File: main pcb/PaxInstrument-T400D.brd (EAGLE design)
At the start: 99.1 x 52.1 mm, 89 parts, among them IC2 NC7S00DBV, J1 MICRO-SDCARD-CONNECTOR-330006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, Q1 DMP2035U-7, U2 APX809, U3 MCP73831, U4 MIC5219-3.3V, X1 FH12-12S-1S, X2 FH12-12S-0.5SH, Y1 RESONATORSMD

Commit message: - Not sure what changed. This is still just playing around.
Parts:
- removed ICSP, ICSP1: ICSP, PaxInstrument-T400:SPARKFUN-CONNECTORS_2X3_SMT_POSTS_PAXINSTRUMENT
- added JP13, JP14, JP15, JP16, JP17: M01PTH, SparkFun-Connectors:1X01
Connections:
- net 3.3V: no longer ICSP1.6
- net DATA1: no longer ICSP1.3
- net DATA2: no longer ICSP1.4
- net GND: no longer ICSP.6, ICSP1.5
- net MISO: now also JP13.1; no longer ICSP.1
- net MOSI: now also JP17.1; no longer ICSP.4
- net RESET: now also JP15.1; no longer ICSP.5
- net SCK: now also JP14.1; no longer ICSP.3
- net SCL: no longer ICSP1.1
- net SDA: no longer ICSP1.2
- net VBUS_IN: now also JP16.1; no longer ICSP.2
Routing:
- net RESET: track 93.9 -> 16.1 mm
- net MOSI: track 127.5 -> 87.6 mm
- net SCK: track 125.8 -> 89.0 mm, vias 4 -> 3
- net MISO: track 111.0 -> 75.6 mm, vias 4 -> 3
- net SCL: track 65.2 -> 31.1 mm, vias 1 -> 0
- net SDA: track 57.5 -> 28.5 mm, vias 1 -> 0
- net VBUS_IN: track 137.4 -> 133.0 mm
- net DATA2: track 58.9 -> 57.9 mm
- net DATA1: track 66.8 -> 66.0 mm
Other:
- board size 99.1 x 52.1 mm -> 99.1 x 71.1 mm

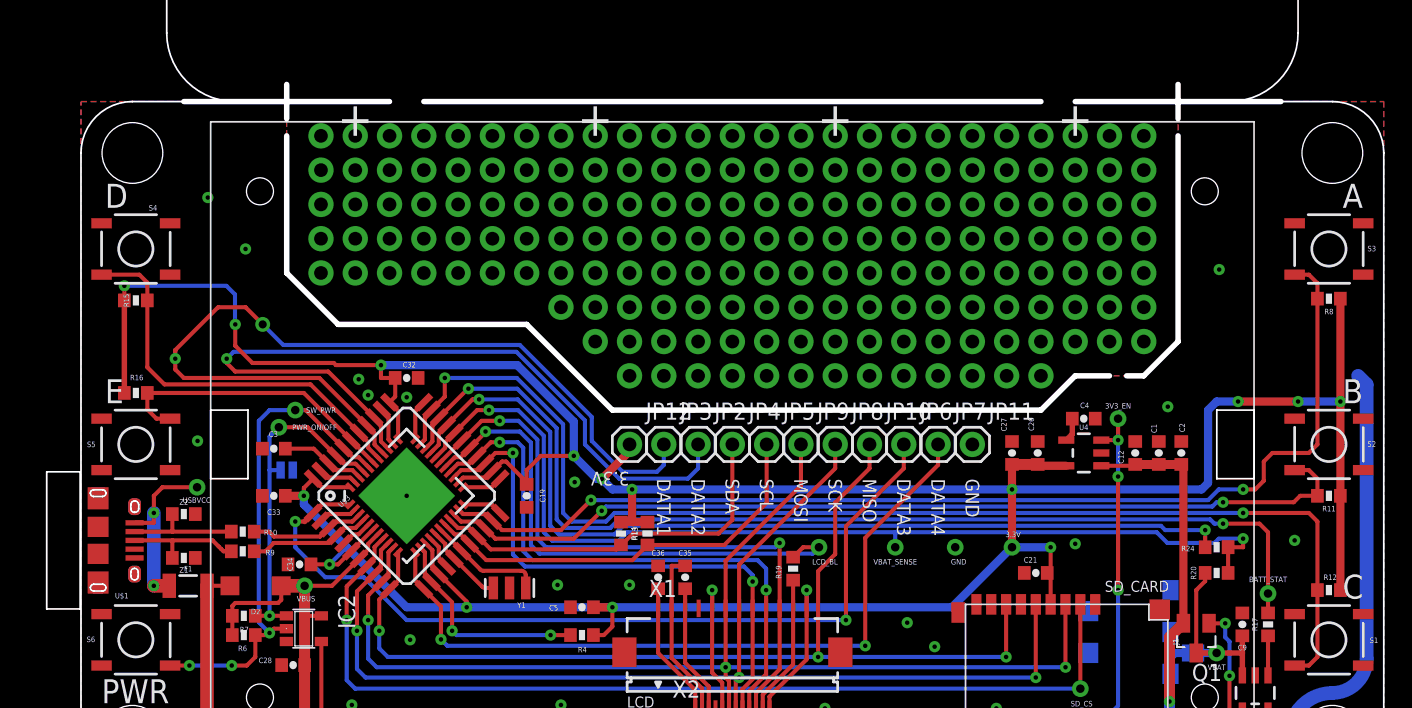
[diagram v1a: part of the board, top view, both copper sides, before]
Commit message: - Moved some components to get more breakout board space. - Increased breakout board size
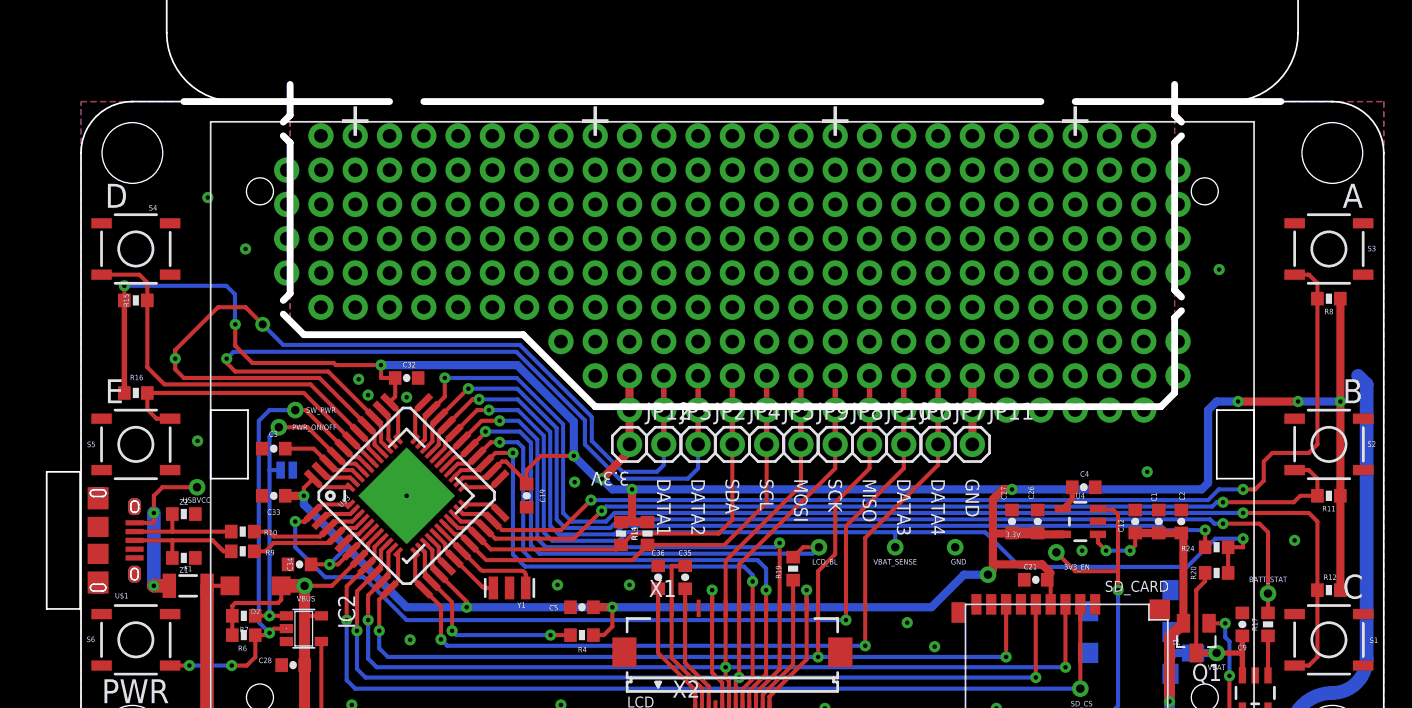
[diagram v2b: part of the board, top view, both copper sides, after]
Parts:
- moved TP2 10.9 mm to (72.3, 17.4)
- moved U4 5.09 mm to (74.0, 19.7)
- moved C1 5.08 mm to (79.9, 19.7)
- moved C12 5.08 mm to (78.1, 19.7)
- moved C2 5.08 mm to (81.5, 19.7)
- moved C26 5.08 mm to (70.9, 19.7)
- moved C27 5.08 mm to (69.0, 19.7)
- moved C4 5.08 mm to (74.3, 22.2)
- moved TP13 2.70 mm to (67.2, 15.7)
- moved C21 0.51 mm to (70.7, 15.4)
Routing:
- net SCK: track 89.0 -> 94.0 mm, vias 3 -> 5
- net MISO: track 75.6 -> 80.7 mm, vias 3 -> 5
- net DATA3: track 64.3 -> 69.4 mm, vias 2 -> 4
- net DATA1: track 66.0 -> 71.0 mm, vias 2 -> 4
- net DATA4: track 56.0 -> 61.1 mm, vias 2 -> 4
- net SDA: track 28.5 -> 33.5 mm, vias 0 -> 2
- net GND: track 17.0 -> 22.1 mm, vias 20 -> 22
- net SCL: track 31.1 -> 36.2 mm, vias 0 -> 2
- net MOSI: track 87.6 -> 92.7 mm, vias 3 -> 5
- net DATA2: track 57.9 -> 62.9 mm, vias 1 -> 3
- net 3.3V: track 283.6 -> 288.5 mm, vias 17 -> 18
- net VBUS: track 121.6 -> 118.7 mm, vias 2 -> 4
- net 3V3EN: track 88.1 -> 86.6 mm, vias 4 -> 2
- net VBAT_SENSE: track 75.3 -> 76.8 mm
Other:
- outline, holes or cut-outs redrawn

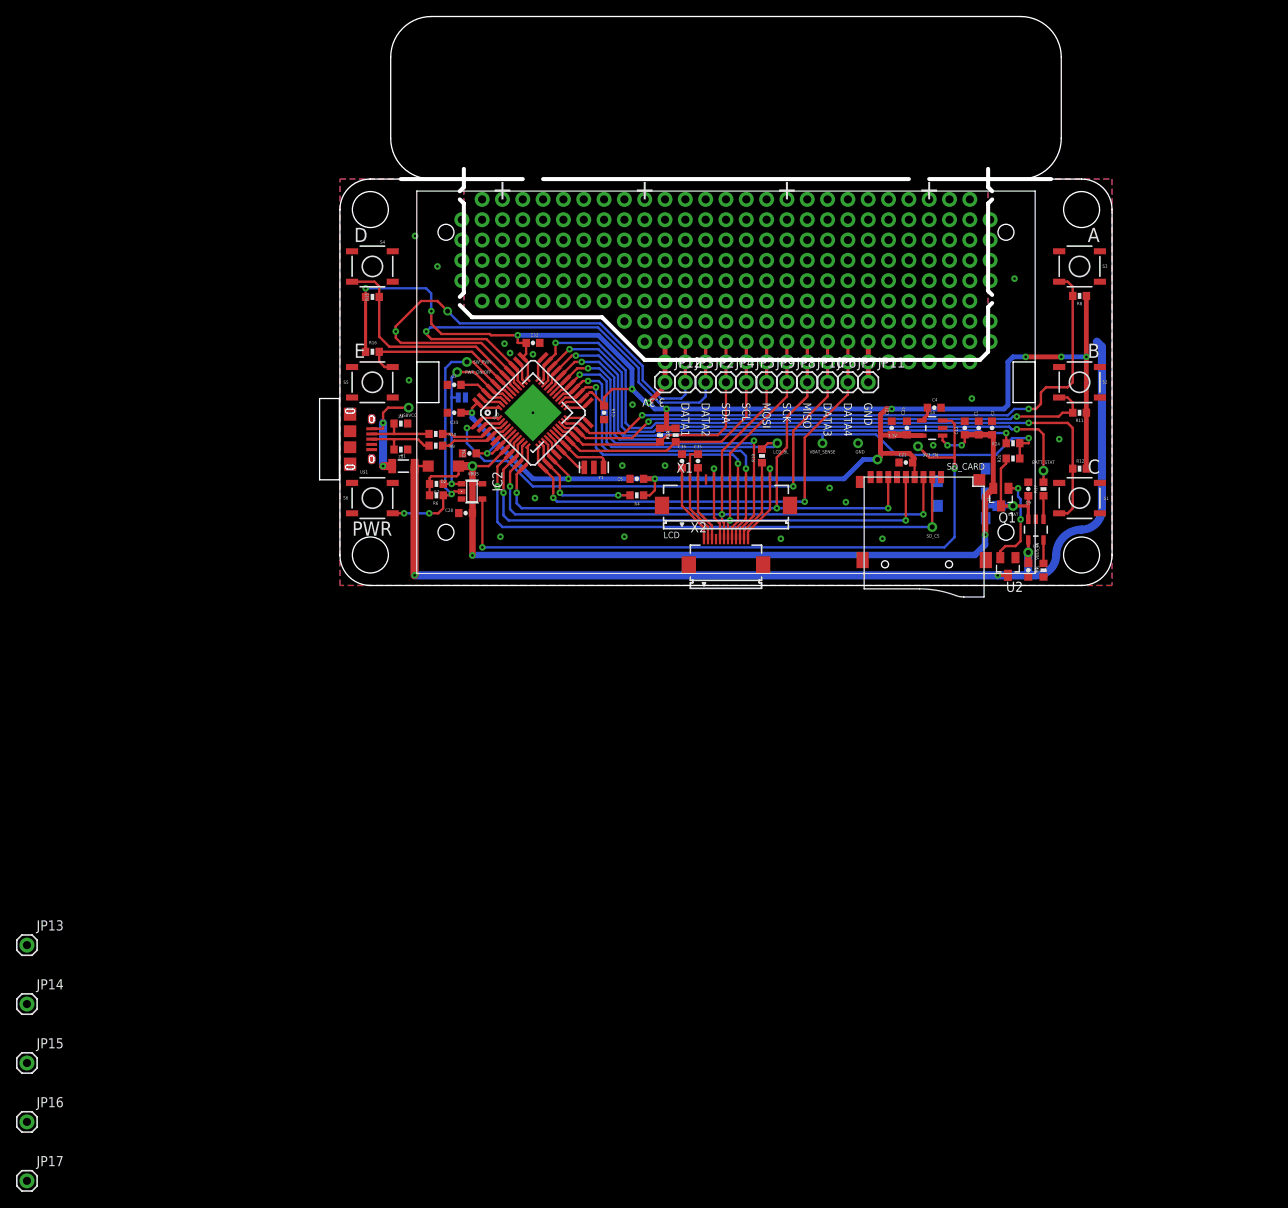
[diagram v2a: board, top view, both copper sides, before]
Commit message: Lengthened the modules.
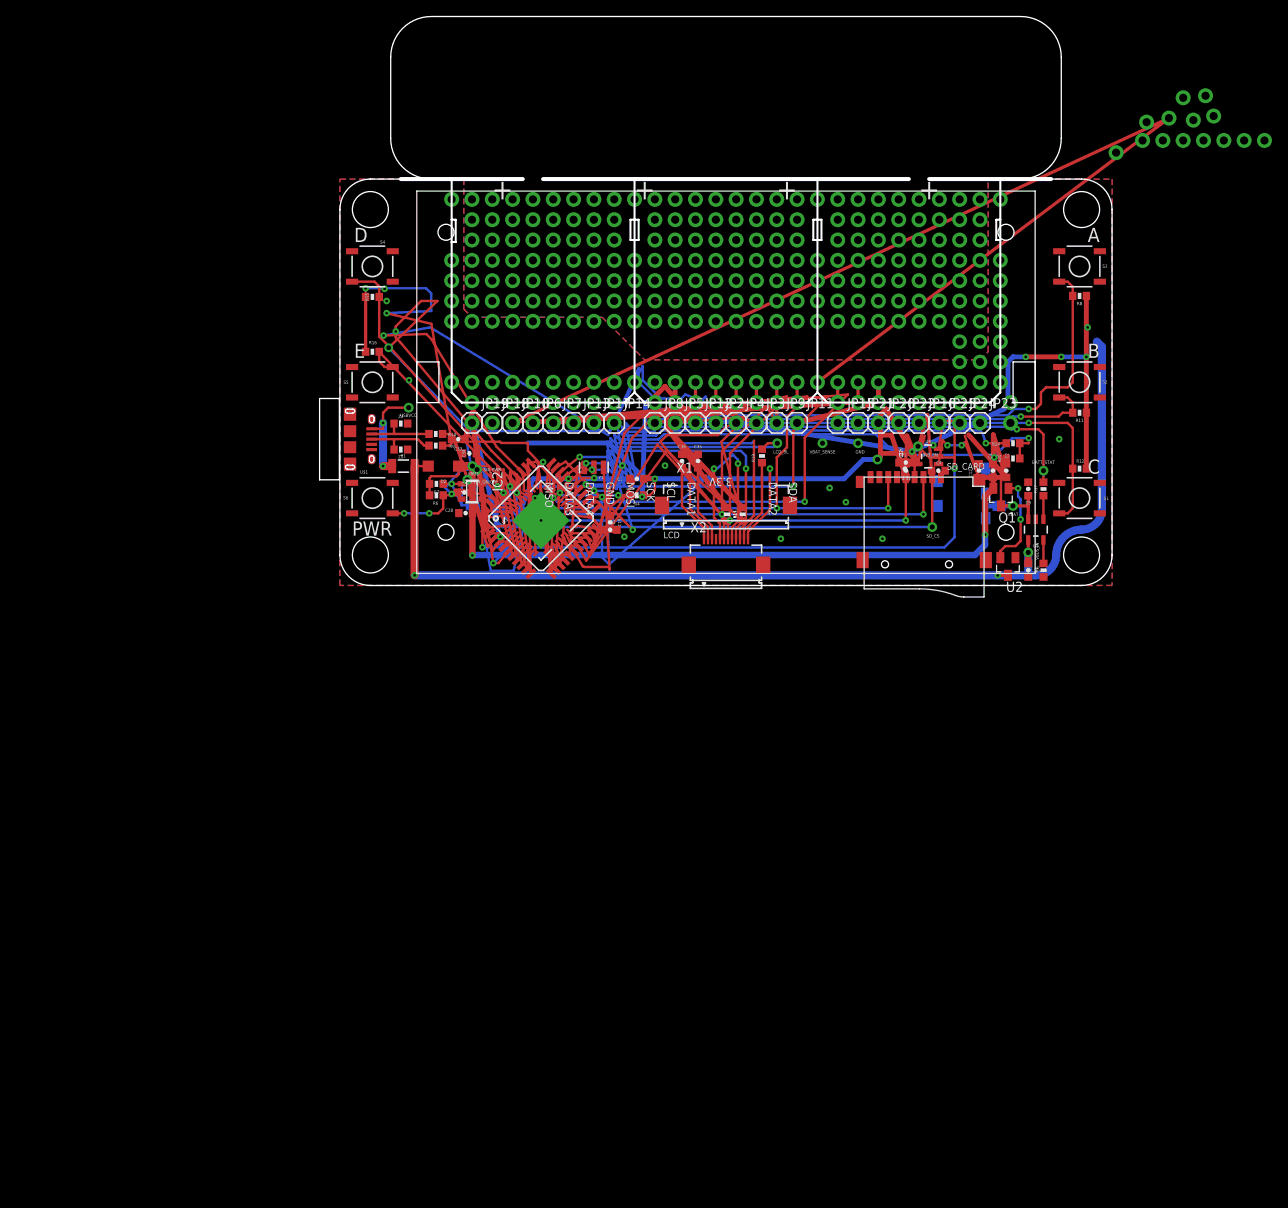
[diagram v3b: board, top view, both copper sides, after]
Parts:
- added JP18, JP19, JP20, JP21, JP22, JP23, JP24, JP25: M01PTH, SparkFun-Connectors:1X01
- moved JP16 141.7 mm to (72.4, 20.3)
- moved JP15 129.1 mm to (62.2, 20.3)
- moved JP17 118.3 mm to (31.8, 20.3)
- moved JP14 103.3 mm to (34.3, 20.3)
- moved JP13 94.5 mm to (29.2, 20.3)
- moved JP10 37.2 mm to (21.6, 20.3)
- moved JP6 37.2 mm to (24.1, 20.3)
- moved JP7 37.2 mm to (26.7, 20.3)
- moved C32 25.3 mm to (33.8, 6.95)
- moved JP8 17.3 mm to (39.4, 20.3)
- moved C19 13.7 mm to (33.8, 7.87)
- moved JP1 13.5 mm to (16.5, 10.0)
- moved TP1 13.5 mm to (17.1, 14.5)
- moved TP9 13.5 mm to (15.9, 13.2)
- moved C3 13.5 mm to (15.6, 11.6)
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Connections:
- new net MOSI2: JP25.1
- new net RESET1: JP23.1
- new net VBUS_IN1: JP24.1
- net MISO: now also JP18.1
- net MOSI: now also JP22.1
- net RESET: now also JP20.1
- net SCK: now also JP19.1
- net VBUS_IN: now also JP21.1
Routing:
- net MISO: track 80.7 -> 290.0 mm
- net 3.3V: track 288.5 -> 452.0 mm, vias 18 -> 14
- net DATA4: track 61.1 -> 164.7 mm
- net DATA3: track 69.4 -> 171.2 mm, vias 4 -> 3
- net DATA1: track 71.0 -> 112.7 mm
- net SCK: track 94.0 -> 134.8 mm
- net SCL: track 36.2 -> 71.1 mm
- net VBUS: track 118.7 -> 148.6 mm
- net SDA: track 33.5 -> 61.9 mm
- net DATA2: track 62.9 -> 90.9 mm
- net SW_C: track 91.1 -> 107.4 mm
- net SW_PWR: track 37.0 -> 24.1 mm
- net XTAL1: track 8.79 -> 20.7 mm
- net LCD_RST: track 43.7 -> 55.5 mm
- net D-: track 8.67 -> 20.0 mm
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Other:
- outline, holes or cut-outs redrawn
